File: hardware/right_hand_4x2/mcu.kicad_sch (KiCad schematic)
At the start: 1 part, among them U1 RP2040-ZERO

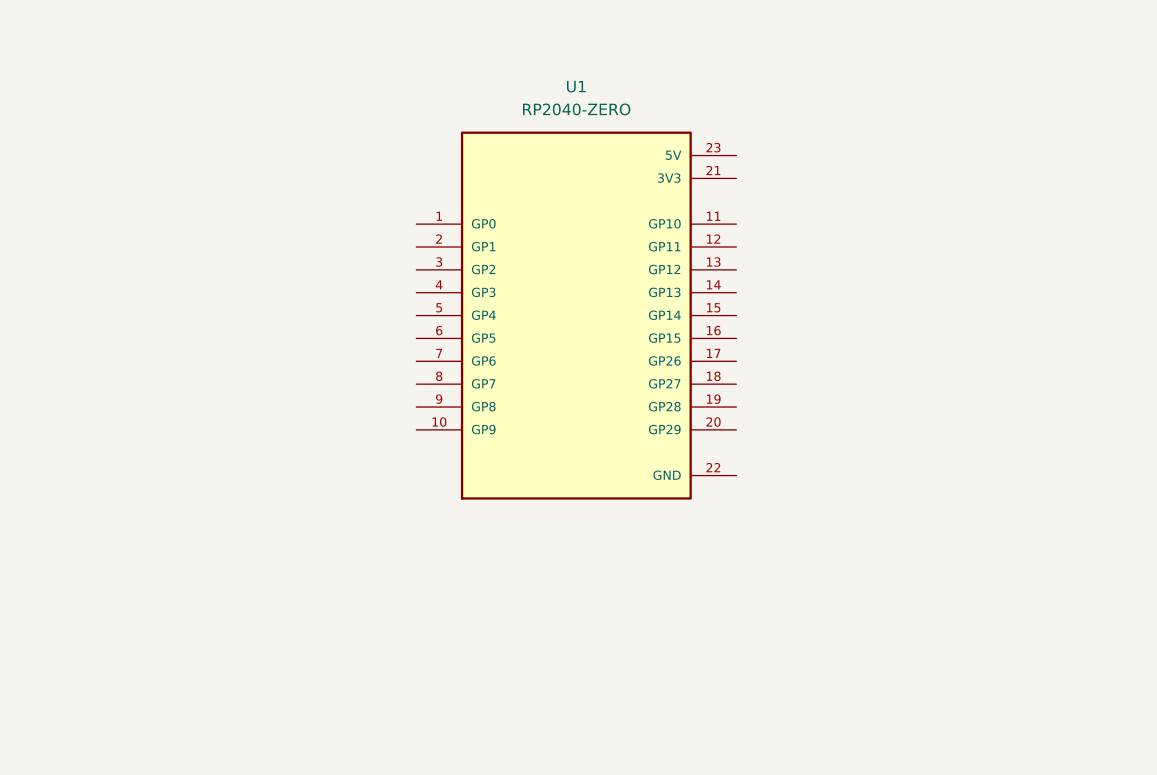
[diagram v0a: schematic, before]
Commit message: 4x2 schematic and layout update
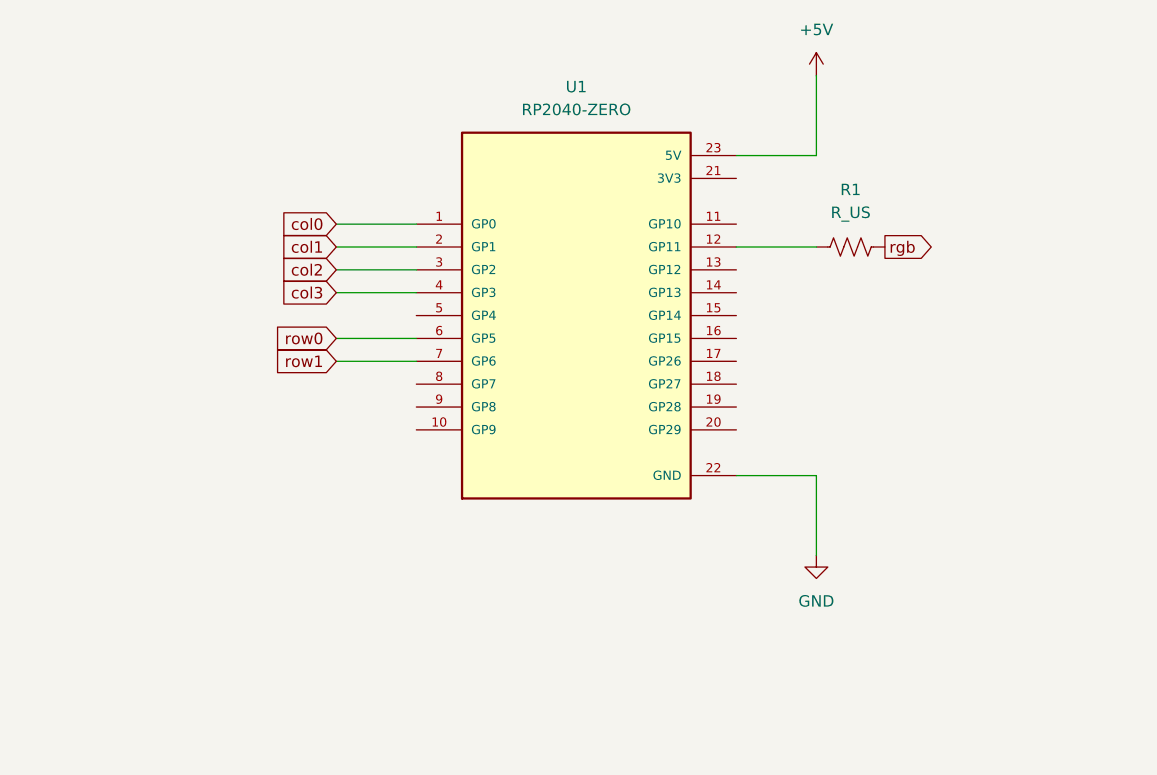
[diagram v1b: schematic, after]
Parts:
- added R1: R_US, Resistor_SMD:R_0805_2012Metric_Pad1.20x1.40mm_HandSolder, symbol Device:R_US
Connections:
- net col0: now reaches U1.1 (GP0)
- net at U1.12 (GP11): now also R1.1
- net col1: now reaches U1.2 (GP1)
- net GND: now reaches U1.22 (GND)
- net +5V: now reaches U1.23 (5V)
- net col2: now reaches U1.3 (GP2)
- net col3: now reaches U1.4 (GP3)
- net row0: now reaches U1.6 (GP5)
- net row1: now reaches U1.7 (GP6)
- new net rgb: R1.2

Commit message: replaced diodes with easier to solder part
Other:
- note added: "Look for the Adafruit QT py rp2040"
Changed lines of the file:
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@@
 	(generator_version "10.0")
 	(paper "A4")
+	(text "Look for the Adafruit QT py rp2040"
+		(exclude_from_sim no)
+		(at 143.764 141.732 0)
+		(effects
+			(font
+				(size 3.81 3.81)
+			)
+		)
+	)
 	(wire
 		(pts
